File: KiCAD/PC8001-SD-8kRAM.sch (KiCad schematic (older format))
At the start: 46 parts, among them J1 PC-8001 ext BUS, J2 AE-microSD-LLCNV, J3 AE-RTC-4543SA-V2, J4 128k MEM CTL, Q1 2SC1815, Q2 2SA1015, Q3 2N7000, SW1 RAM SW, U1 74HC04, U2 74HC32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

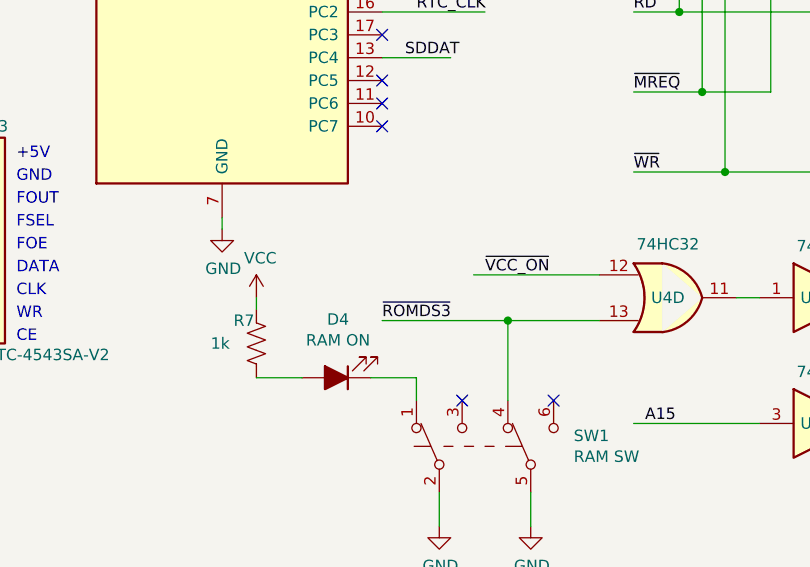
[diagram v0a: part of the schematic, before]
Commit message: ROMDS3切り離し用ジャンパパッド追加
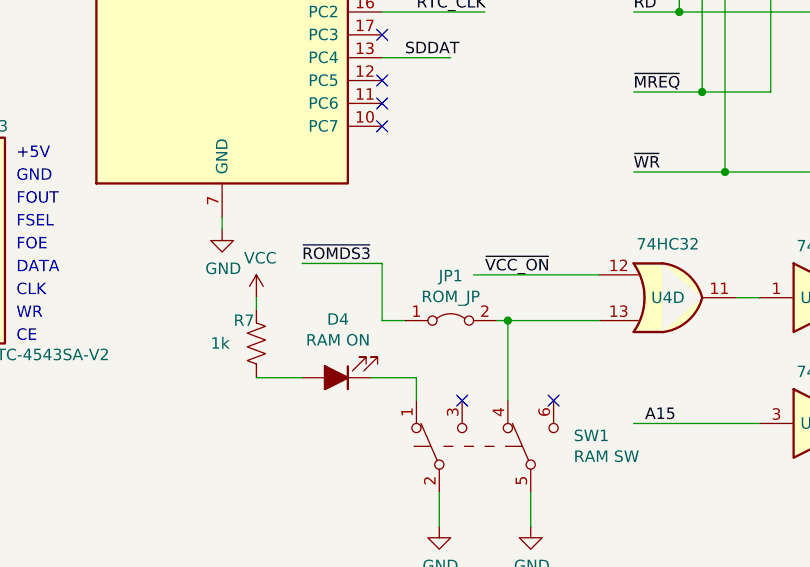
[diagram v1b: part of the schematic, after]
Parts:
- added JP1: ROM_JP, Jumper:SolderJumper-2_P1.3mm_Bridged_RoundedPad1.0x1.5mm, symbol Jumper:Jumper_2_Bridged
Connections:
- wire segments 333 -> 336
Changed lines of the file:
@@
 	6300 5750 6300 5900
 Wire Wire Line
-	6050 5000 6600 5000
-Connection ~ 6600 5000
-Text Label 6050 5000 0    50   ~ 0
+	5700 4750 6050 4750
+Text Label 5700 4750 0    50   ~ 0
 ~ROMDS3
 $Comp
@@
 	1    0    0    -1
 $EndComp
+$Comp
+L Jumper:Jumper_2_Bridged JP1
+U 1 1 613AC2B8
+P 6350 5000
+F 0 "JP1" H 6350 5195 50  0000 C CNN
+F 1 "ROM_JP" H 6350 5104 50  0000 C CNN
+F 2 "Jumper:SolderJumper-2_P1.3mm_Bridged_RoundedPad1.0x1.5mm" H 6350 5000 50  0001 C CNN
+F 3 "~" H 6350 5000 50  0001 C CNN
+	1    6350 5000
+	1    0    0    -1
+$EndComp
+Wire Wire Line
+	6050 4750 6050 5000
+Wire Wire Line
+	6050 5000 6150 5000
+Wire Wire Line
+	6550 5000 6600 5000
+Connection ~ 6600 5000
 $EndSCHEMATC

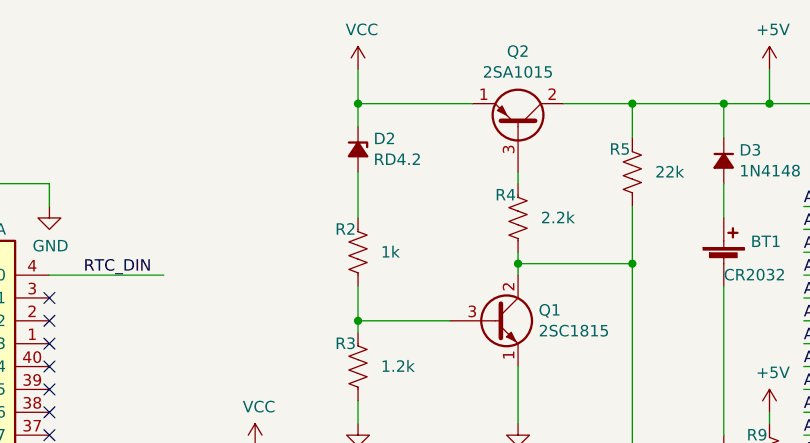
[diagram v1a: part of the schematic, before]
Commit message: 回路図のツェナーダイオード定格を変更 RD4.2→RD3.6
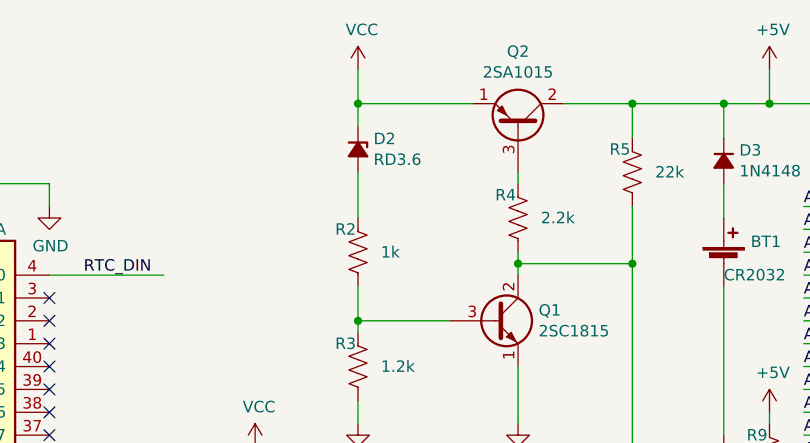
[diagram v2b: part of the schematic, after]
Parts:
- D2: value RD4.2 -> RD3.6
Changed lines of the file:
@@
 EESchema Schematic File Version 4
-LIBS:PC8001-SD-8kRAM-cache
 EELAYER 30 0
 EELAYER END
@@
 P 7400 1100
 F 0 "D2" V 7354 1168 50  0000 L CNN
-F 1 "RD4.2" V 7445 1168 50  0000 L CNN
+F 1 "RD3.6" V 7445 1168 50  0000 L CNN
 F 2 "Diode_THT:D_DO-34_SOD68_P7.62mm_Horizontal" V 7400 1100 50  0001 C CNN
 F 3 "~" V 7400 1100 50  0001 C CNN
